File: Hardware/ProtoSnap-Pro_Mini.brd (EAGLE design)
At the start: 39.4 x 63.5 mm, 66 parts, among them Q1 16MHz, U1 ATMEGA328, U2 MIC5205, U3 FT232RLSSOP, U4 TEMT6000, X2 USB-SMD-NS

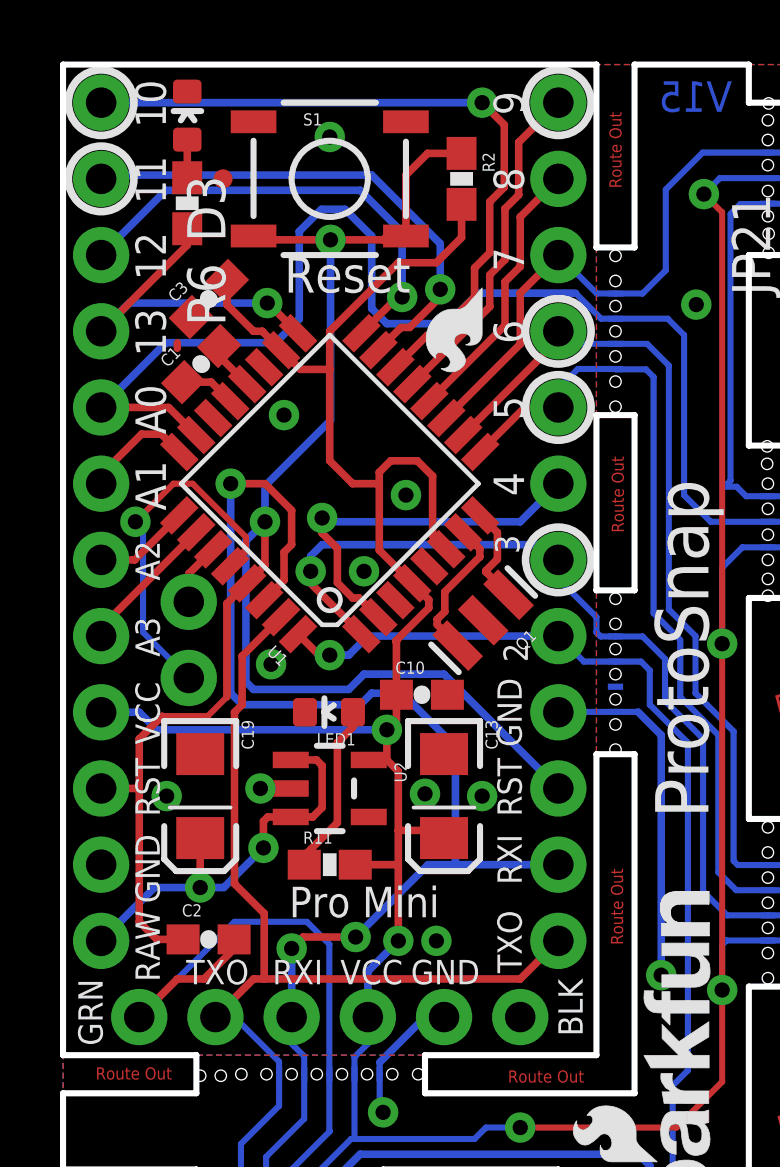
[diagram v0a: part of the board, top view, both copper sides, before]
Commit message: Rotated Oscillator to verticle position Had to nudge many other nearby components to make room. Also re-routed as necessary
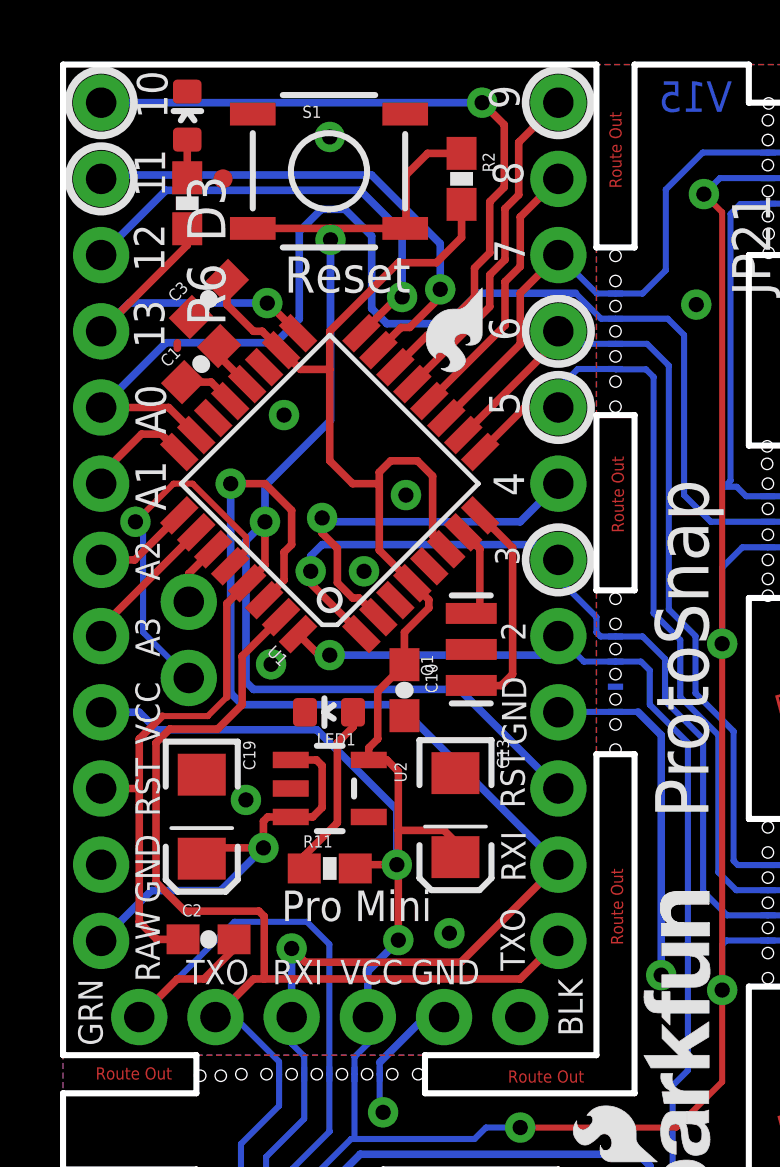
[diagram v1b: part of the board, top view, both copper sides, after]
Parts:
- moved Q1 1.05 mm to (13.6, 44.0), turned to 90 degrees
- moved C13 0.74 mm to (13.1, 38.5)
- moved C19 0.69 mm to (4.62, 38.4)
- moved C10 0.60 mm to (11.4, 42.6), turned to 270 degrees
- moved S1 0.26 mm to (8.86, 59.9)
- moved R11 0.13 mm to (8.89, 36.7)
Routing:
- net RX-I: track 45.4 -> 49.9 mm
- net VCC: track 182.6 -> 186.9 mm
- net N$1: track 3.35 -> 7.28 mm
- net N$2: track 4.88 -> 3.15 mm
- net TX-O: track 53.1 -> 54.3 mm, vias 3 -> 2
- net RAW: track 13.9 -> 15.0 mm, vias 2 -> 1
- net GND: track 79.3 -> 78.3 mm, vias 19 -> 16

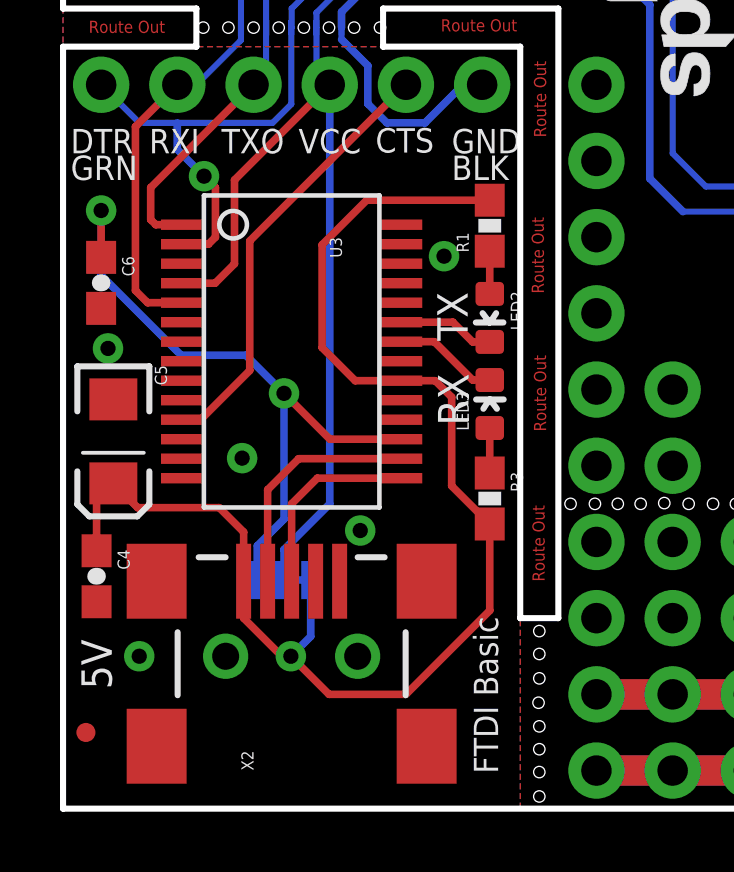
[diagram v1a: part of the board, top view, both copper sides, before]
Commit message: Moved caps on FTDI Basic to avoid depanlization damage Also re-routed 5V net to more directly route to IC
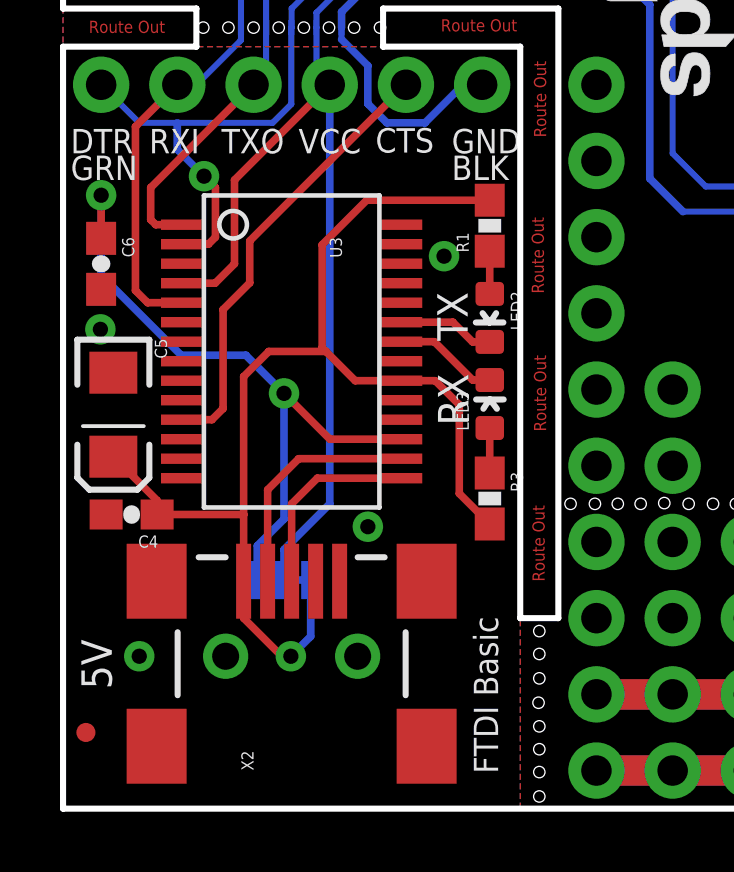
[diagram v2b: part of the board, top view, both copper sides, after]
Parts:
- moved C4 2.37 mm to (2.29, 9.80), turned to 180 degrees
- moved C5 0.89 mm to (1.68, 13.1)
- moved C6 0.64 mm to (1.27, 18.2)
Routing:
- net 5V: track 46.2 -> 40.9 mm
- net GND: vias 16 -> 15
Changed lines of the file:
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@@
 <setting verticaltext="up"/>
 </settings>
-<grid distance="0.05" unitdist="inch" unit="inch" style="lines" multiple="1" display="yes" altdistance="0.001" altunitdist="inch" altunit="inch"/>
+<grid distance="0.05" unitdist="inch" unit="inch" style="lines" multiple="1" display="yes" altdistance="0.005" altunitdist="inch" altunit="inch"/>
 <layers>
 <layer number="1" name="Top" color="4" fill="1" visible="yes" active="yes"/>
@@
 <layer number="27" name="tValues" color="7" fill="1" visible="no" active="yes"/>
 <layer number="28" name="bValues" color="7" fill="1" visible="no" active="yes"/>
-<layer number="29" name="tStop" color="7" fill="3" visible="no" active="yes"/>
+<layer number="29" name="tStop" color="7" fill="3" visible="yes" active="yes"/>
 <layer number="30" name="bStop" color="7" fill="6" visible="no" active="yes"/>
 <layer number="31" name="tCream" color="7" fill="4" visible="no" active="yes"/>
@@
 <element name="JP1" library="SparkFun" package="1X06" value="FTDI Basic" x="2.54" y="31.75" rot="MR180"/>
 <element name="C2" library="SparkFun" package="0603-CAP" value="0.1uF" x="4.8514" y="34.3408"/>
-<element name="C4" library="SparkFun" package="0603-CAP" value="0.1uF" x="1.1176" y="7.747" smashed="yes" rot="R270">
-<attribute name="NAME" x="1.8161" y="8.636" size="0.4064" layer="25" rot="R270"/>
-<attribute name="VALUE" x="-0.0254" y="8.8265" size="0.4064" layer="27" rot="R270"/>
-</element>
-<element name="C5" library="SparkFun" package="EIA3216" value="10uF" x="1.6764" y="12.2428" smashed="yes" rot="R270">
-<attribute name="NAME" x="3.0574" y="14.7828" size="0.4064" layer="25" rot="R270"/>
-<attribute name="VALUE" x="3.0084" y="11.8348" size="0.4064" layer="27" rot="R270"/>
-</element>
-<element name="C6" library="SparkFun" package="0603-CAP" value="0.1uF" x="1.27" y="17.526" smashed="yes" rot="R270">
-<attribute name="NAME" x="1.9685" y="18.415" size="0.4064" layer="25" rot="R270"/>
-<attribute name="VALUE" x="0.127" y="18.6055" size="0.4064" layer="27" rot="R270"/>
+<element name="C4" library="SparkFun" package="0603-CAP" value="0.1uF" x="2.286" y="9.8044" smashed="yes" rot="R180">
+<attribute name="NAME" x="3.175" y="9.1059" size="0.4064" layer="25" rot="R180"/>
+<attribute name="VALUE" x="3.3655" y="10.9474" size="0.4064" layer="27" rot="R180"/>
+</element>
+<element name="C5" library="SparkFun" package="EIA3216" value="10uF" x="1.6764" y="13.1318" smashed="yes" rot="R270">
+<attribute name="NAME" x="3.0574" y="15.6718" size="0.4064" layer="25" rot="R270"/>
+<attribute name="VALUE" x="3.0084" y="12.7238" size="0.4064" layer="27" rot="R270"/>
+</element>
+<element name="C6" library="SparkFun" package="0603-CAP" value="0.1uF" x="1.27" y="18.161" smashed="yes" rot="R270">
+<attribute name="NAME" x="1.9685" y="19.05" size="0.4064" layer="25" rot="R270"/>
+<attribute name="VALUE" x="0.127" y="19.2405" size="0.4064" layer="27" rot="R270"/>
 </element>
 <element name="X2" library="SparkFun" package="USB-MINIB-NOSTOP" value="USB-SMD-NS" x="7.62" y="5.08" smashed="yes" rot="R90">
@@
 <via x="12.7" y="18.415" extent="1-16" drill="0.508"/>
 <via x="2.54" y="5.08" extent="1-16" drill="0.508"/>
-<via x="9.906" y="9.271" extent="1-16" drill="0.508"/>
-<via x="1.4986" y="15.3416" extent="1-16" drill="0.508"/>
-<via x="5.969" y="11.684" extent="1-16" drill="0.508"/>
+<via x="10.16" y="9.398" extent="1-16" drill="0.508"/>
+<via x="1.2446" y="15.9766" extent="1-16" drill="0.508"/>
 <via x="10.668" y="28.575" extent="1-16" drill="0.508"/>
 <via x="30.48" y="50.8" extent="1-16" drill="0.508"/>
@@
 <contactref element="U3" pad="11"/>
 <contactref element="JP3" pad="2"/>
-<wire x1="3.964" y1="12.965" x2="4.583" y2="12.965" width="0.254" layer="1"/>
+<wire x1="3.964" y1="12.965" x2="4.964" y2="12.965" width="0.254" layer="1"/>
 <wire x1="6.223" y1="18.923" x2="11.43" y2="24.13" width="0.254" layer="1"/>
-<wire x1="6.223" y1="14.605" x2="6.223" y2="18.923" width="0.254" layer="1"/>
-<wire x1="4.583" y1="12.965" x2="6.223" y2="14.605" width="0.254" layer="1"/>
+<wire x1="6.223" y1="17.526" x2="6.223" y2="18.923" width="0.254" layer="1"/>
+<wire x1="5.334" y1="16.637" x2="6.223" y2="17.526" width="0.254" layer="1"/>
+<wire x1="5.334" y1="16.637" x2="5.334" y2="13.335" width="0.254" layer="1"/>
+<wire x1="5.334" y1="13.335" x2="4.964" y2="12.965" width="0.254" layer="1"/>
 </signal>
 <signal name="3.3V" class="1">
@@
 <wire x1="7.366" y1="13.843" x2="6.096" y2="15.113" width="0.254" layer="16"/>
 <wire x1="6.096" y1="15.113" x2="3.937" y2="15.113" width="0.254" layer="16"/>
-<wire x1="1.27" y1="17.78" x2="1.27" y2="19.939" width="0.254" layer="16"/>
+<wire x1="1.27" y1="17.78" x2="1.27" y2="20.447" width="0.254" layer="16"/>
 <wire x1="3.937" y1="15.113" x2="1.27" y2="17.78" width="0.254" layer="16"/>
-<wire x1="1.27" y1="19.939" x2="1.27" y2="18.376" width="0.254" layer="1"/>
+<wire x1="1.27" y1="20.447" x2="1.27" y2="19.011" width="0.254" layer="1"/>
 <via x="7.366" y="13.843" extent="1-16" drill="0.508"/>
-<via x="1.27" y="19.939" extent="1-16" drill="0.508"/>
+<via x="1.27" y="20.447" extent="1-16" drill="0.508"/>
 </signal>
 <signal name="TXLED">
@@
 <contactref element="R3" pad="2"/>
 <wire x1="12.405" y1="14.265" x2="11.276" y2="14.265" width="0.254" layer="1"/>
-<wire x1="12.954" y1="13.716" x2="12.405" y2="14.265" width="0.254" layer="1"/>
-<wire x1="9.738" y1="14.265" x2="8.636" y2="15.367" width="0.254" layer="1"/>
+<wire x1="13.208" y1="13.462" x2="12.405" y2="14.265" width="0.254" layer="1"/>
+<wire x1="9.738" y1="14.265" x2="8.763" y2="15.24" width="0.254" layer="1"/>
+<wire x1="8.763" y1="15.24" x2="8.636" y2="15.367" width="0.254" layer="1"/>
 <wire x1="8.636" y1="18.796" x2="10.121" y2="20.281" width="0.254" layer="1"/>
 <wire x1="8.636" y1="15.367" x2="8.636" y2="18.796" width="0.254" layer="1"/>
@@
 <via x="7.5946" y="5.08" extent="1-16" drill="0.508"/>
 <wire x1="14.224" y1="20.281" x2="10.121" y2="20.281" width="0.254" layer="1"/>
-<wire x1="12.954" y1="13.716" x2="12.954" y2="10.7578" width="0.254" layer="1"/>
-<wire x1="12.954" y1="10.7578" x2="14.224" y2="9.4878" width="0.254" layer="1"/>
-<wire x1="11.43" y1="3.81" x2="14.224" y2="6.604" width="0.254" layer="1"/>
-<wire x1="14.224" y1="6.604" x2="14.224" y2="9.4878" width="0.254" layer="1"/>
-<wire x1="1.1176" y1="8.597" x2="1.1176" y2="10.8428" width="0.254" layer="1"/>
-<wire x1="1.1176" y1="10.8428" x2="1.6764" y2="10.8428" width="0.254" layer="1"/>
-<wire x1="6.02" y1="9.22" x2="6.02" y2="7.58" width="0.254" layer="1"/>
+<wire x1="13.208" y1="10.5038" x2="14.224" y2="9.4878" width="0.254" layer="1"/>
 <wire x1="6.02" y1="7.62" x2="6.02" y2="7.58" width="0.254" layer="1"/>
 <wire x1="6.02" y1="6.35" x2="6.02" y2="7.58" width="0.254" layer="1"/>
 <wire x1="8.255" y1="7.62" x2="8.255" y2="5.7404" width="0.254" layer="16"/>
 <wire x1="8.255" y1="5.7404" x2="7.5946" y2="5.08" width="0.254" layer="16"/>
-<wire x1="11.43" y1="3.81" x2="8.8646" y2="3.81" width="0.254" layer="1"/>
-<wire x1="8.8646" y1="3.81" x2="7.5946" y2="5.08" width="0.254" layer="1"/>
 <wire x1="7.5946" y1="5.08" x2="7.29" y2="5.08" width="0.254" layer="1"/>
 <wire x1="7.29" y1="5.08" x2="6.02" y2="6.35" width="0.254" layer="1"/>
-<wire x1="6.02" y1="9.22" x2="5.207" y2="10.033" width="0.254" layer="1"/>
-<wire x1="5.207" y1="10.033" x2="2.4862" y2="10.033" width="0.254" layer="1"/>
-<wire x1="2.4862" y1="10.033" x2="1.6764" y2="10.8428" width="0.254" layer="1"/>
+<wire x1="6.02" y1="9.8044" x2="3.136" y2="9.8044" width="0.254" layer="1"/>
+<wire x1="1.6764" y1="11.7318" x2="3.136" y2="10.2722" width="0.254" layer="1"/>
+<wire x1="3.136" y1="10.2722" x2="3.136" y2="9.8044" width="0.254" layer="1"/>
+<wire x1="6.02" y1="7.58" x2="6.02" y2="9.8044" width="0.254" layer="1"/>
+<wire x1="6.02" y1="9.8044" x2="6.02" y2="14.402" width="0.254" layer="1"/>
+<wire x1="6.02" y1="14.402" x2="6.858" y2="15.24" width="0.254" layer="1"/>
+<wire x1="6.858" y1="15.24" x2="8.763" y2="15.24" width="0.254" layer="1"/>
+<wire x1="13.208" y1="13.462" x2="13.208" y2="10.5038" width="0.254" layer="1"/>
 </signal>
 <signal name="N$6">

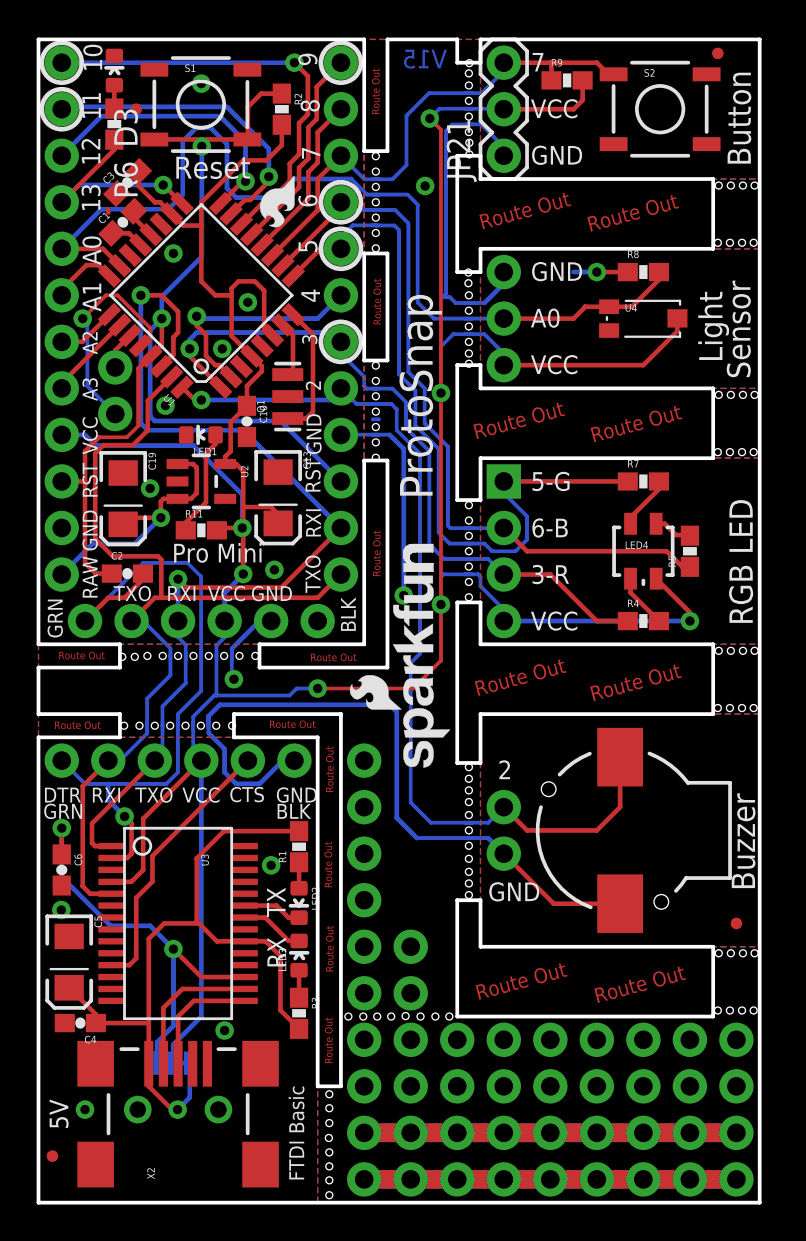
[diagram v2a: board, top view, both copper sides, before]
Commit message: Updated packages on resonator, buttons and leds
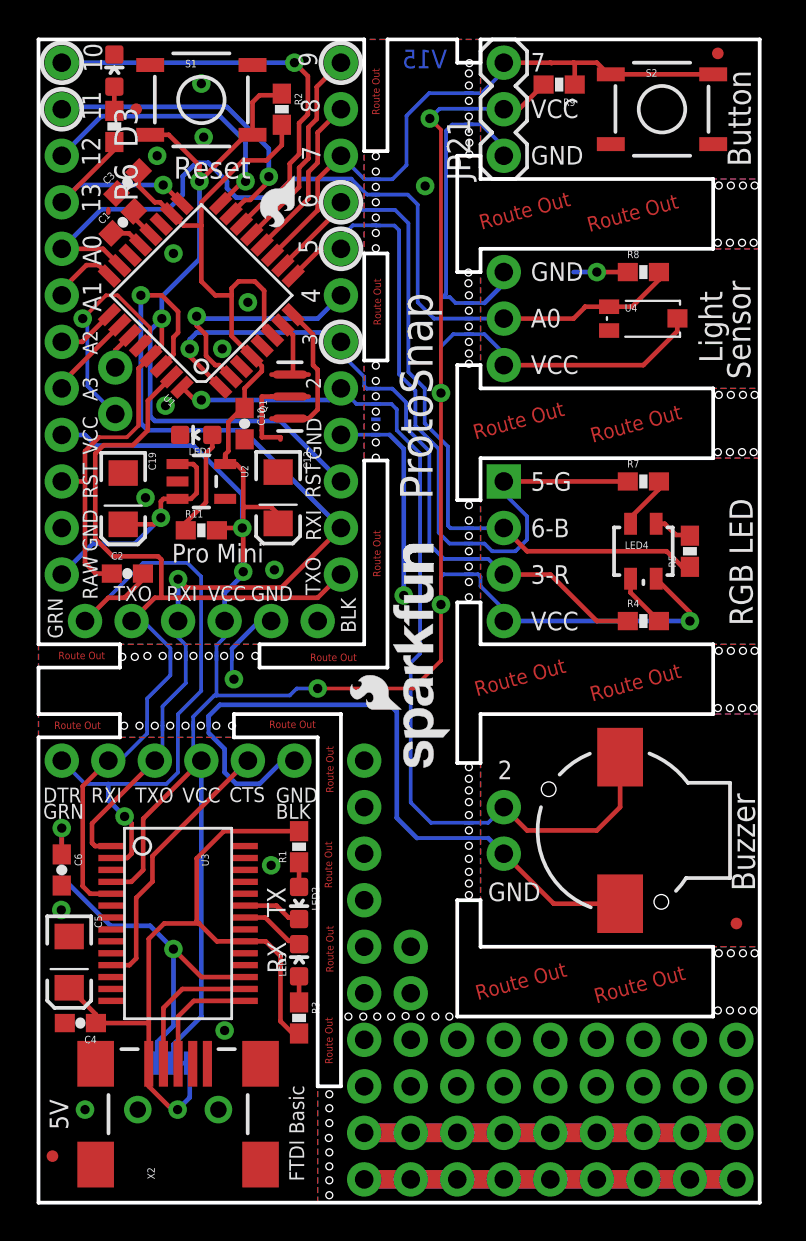
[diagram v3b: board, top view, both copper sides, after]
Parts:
- D3, LED1, LED2, LED3: device SparkFun-LED:LED-0603-QC -> Testing:0603-LED-ALT1
- Q1: device SparkFun:RESONATOR-SMD -> Testing:RESONATOR-SMD-1:1
- S1: value Reset -> (none); device SparkFun:TACTILE_SWITCH_SMD -> Testing:TACTILE-SWITCH-SMD-ALT01
- S2: value SWITCH-MOMENTARY-2SMD -> (none); device SparkFun:TACTILE_SWITCH_SMD -> Testing:TACTILE-SWITCH-SMD-ALT01
- moved R9 0.49 mm to (28.4, 61.0), turned to 180 degrees
- moved S1 0.26 mm to (8.89, 60.2)
- moved LED1 0.25 mm to (8.61, 41.9)
- moved LED3 0.25 mm to (14.2, 13.2)
- moved R3 0.25 mm to (14.2, 10.1)
- moved C10 0.18 mm to (11.3, 42.5)
- moved R6 0.13 mm to (4.14, 58.8)
- moved Q1 0.13 mm to (13.7, 44.0)
- moved S2 0.10 mm to (34.0, 59.7)
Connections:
- net D7: now also S2.2
- net GND: now also S2.4
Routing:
- net D7: track 28.1 -> 33.9 mm
- net GND: track 78.3 -> 82.2 mm, vias 15 -> 17
- net A0: track 51.6 -> 47.7 mm
- net VCC: track 186.9 -> 184.6 mm
- net N$1: track 7.28 -> 6.43 mm
- net RAW: track 15.0 -> 14.5 mm
